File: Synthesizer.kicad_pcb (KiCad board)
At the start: 6 copper layers, 135.2 x 94.2 mm, 155 parts, among them J1 USB_A, J2 AudioJack3, J3 USB_B_Micro, J4 FPGA_debug, J5 MCU_debug, J6 MCU_GPIO, J7 FPGA_GPIO, SW1 SW_Push, SW10 SW_Push, SW11 SW_Push, SW12 SW_Push, SW13 SW_Push, SW14 SW_Push, SW15 SW_Push, SW16 SW_Push, SW2 SW_Push, SW3 SW_Push, SW4 SW_Push, SW5 SW_Push, SW6 SW_Push, SW7 SW_Push, SW8 SW_Push, SW9 SW_Push, U1 TPD3S014, U2 S25FL127S, U3 XC7A100T-FTG256, U4 Oscillator, U5 TPS54325, U6 TPS54294, U7 EFM32GG11B4xx, U8 PCM5102, Y1 48Mhz

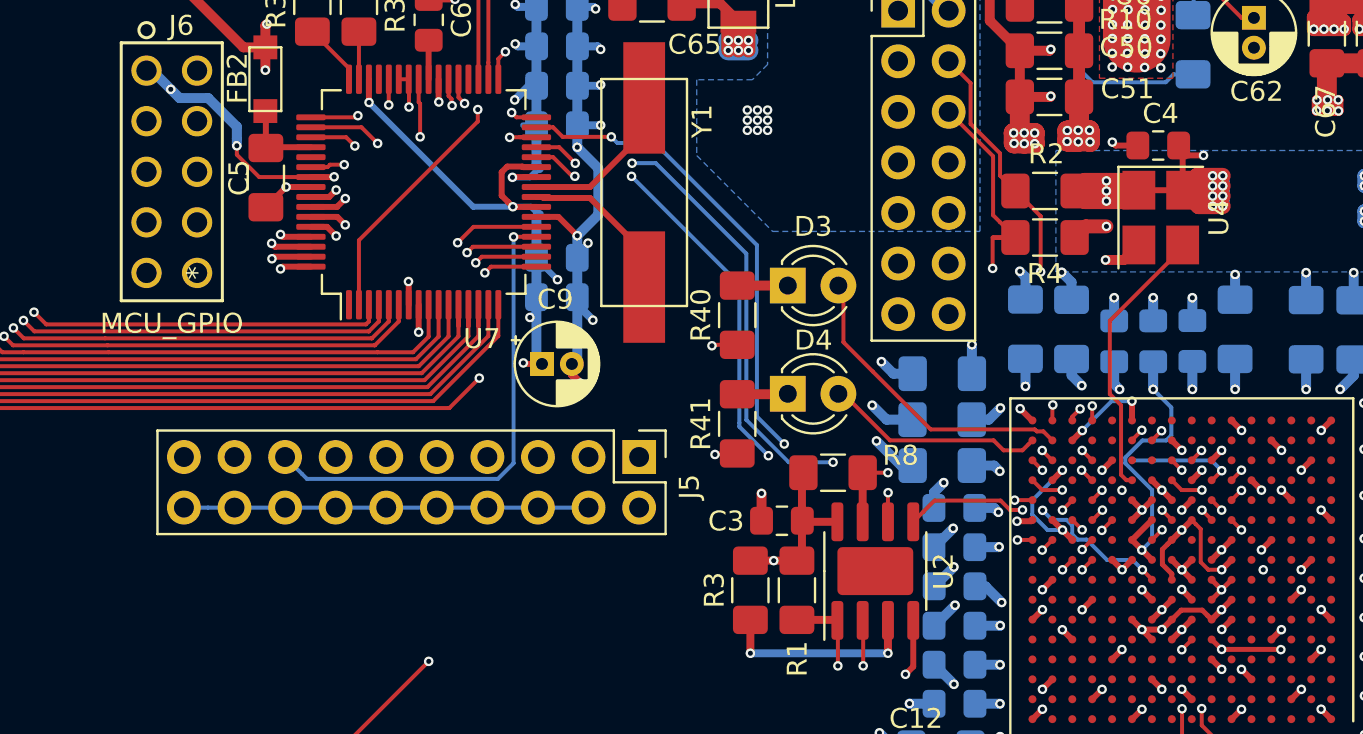
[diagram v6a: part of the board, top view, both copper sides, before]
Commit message: Thicken traces and thin planes
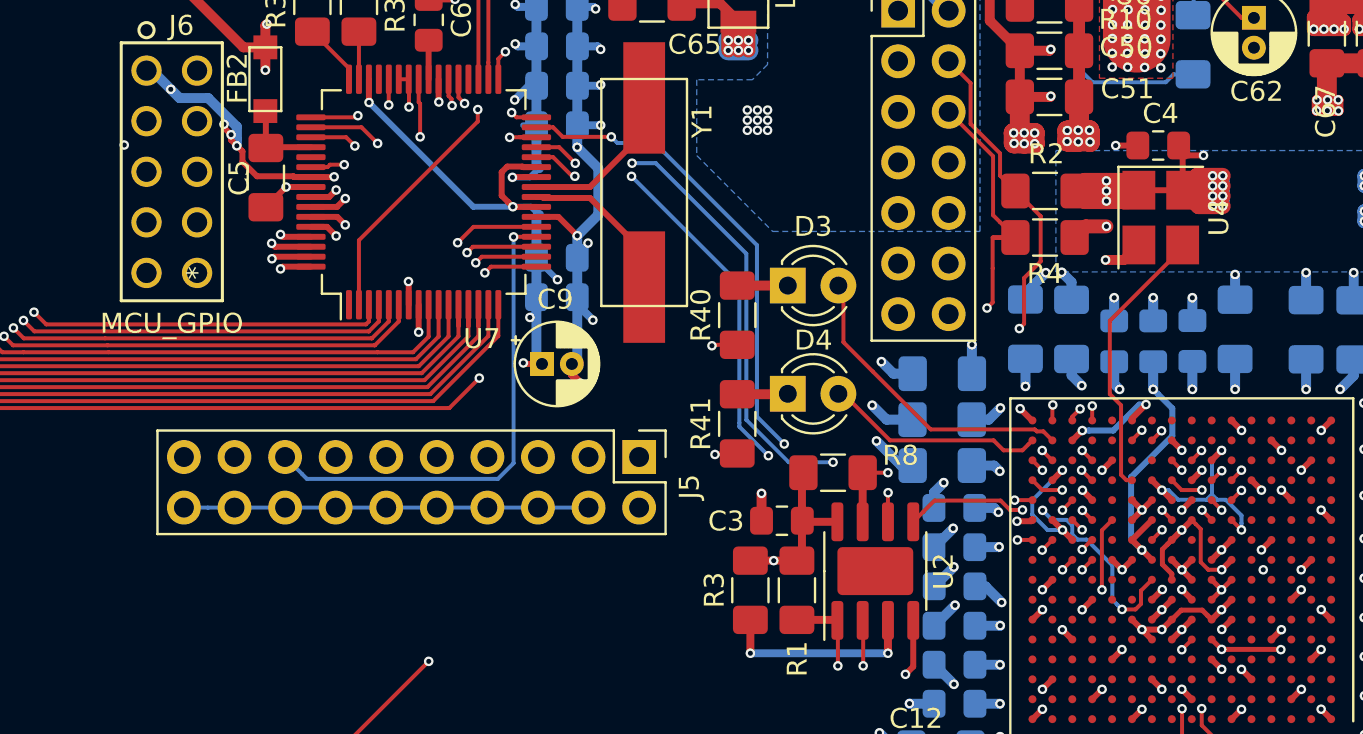
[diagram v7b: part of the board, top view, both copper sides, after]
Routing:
- net +3V3: track 504.1 -> 526.4 mm, vias 119 -> 122
- net Net-(J4-Pad10): track 26.8 -> 22.1 mm
- net +1V8: track 51.3 -> 48.9 mm
- net Net-(J4-Pad8): track 23.7 -> 22.2 mm
- net Net-(J4-Pad4): track 32.3 -> 31.0 mm
- net /Artix7/DAC_LRCK: track 49.2 -> 50.2 mm
- net /EFM32/FPGA_Ready: track 59.6 -> 60.2 mm
- net Net-(R1-Pad2): track 23.1 -> 23.7 mm
- net Net-(J4-Pad6): track 31.1 -> 31.3 mm, vias 3 -> 2

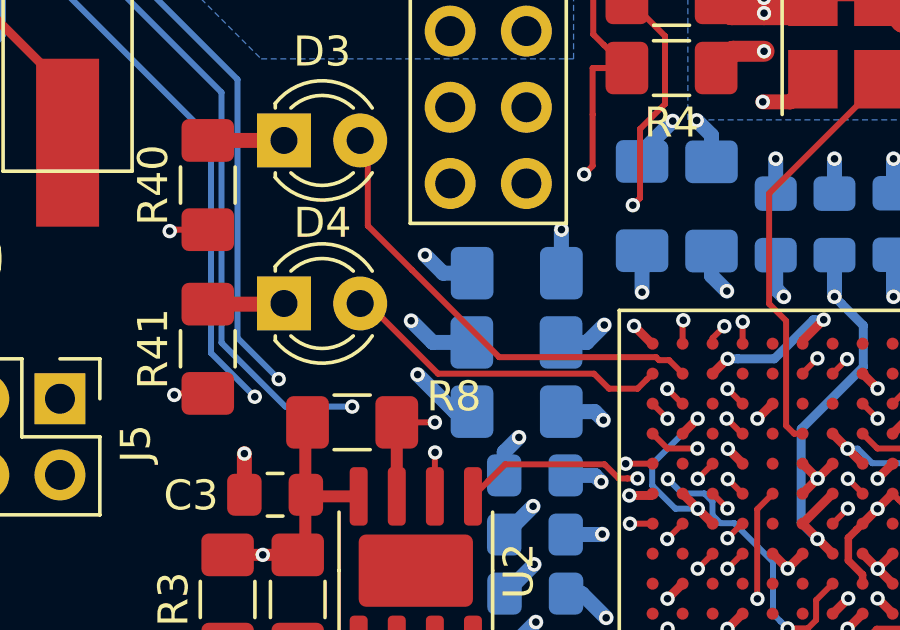
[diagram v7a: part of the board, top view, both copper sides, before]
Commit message: Thicken 1.8V layer
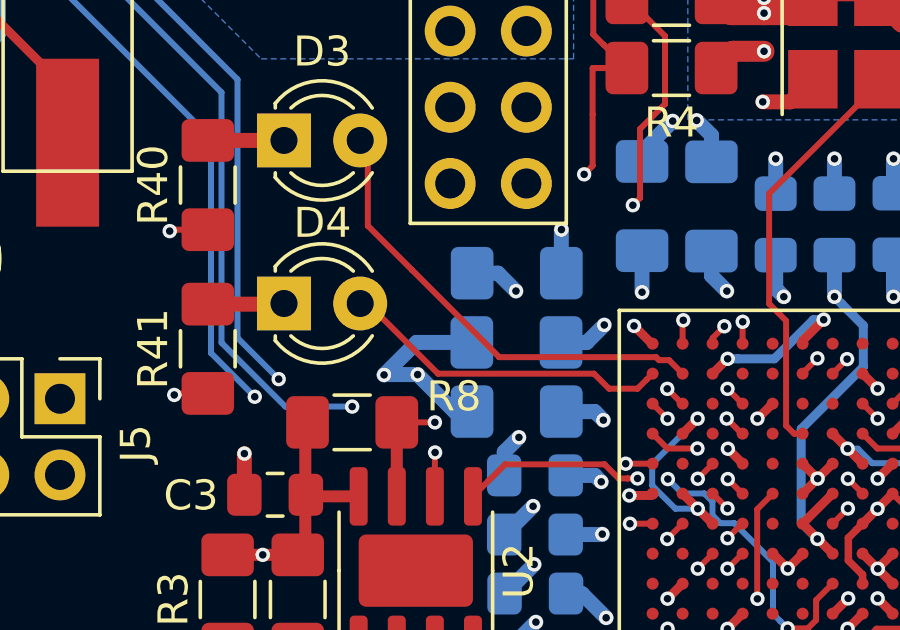
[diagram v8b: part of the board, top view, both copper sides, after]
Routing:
- net GND: track 360.0 -> 362.1 mm
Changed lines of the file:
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@@
     (thickness 1.6)
     (drawings 4)
-    (tracks 2591)
+    (tracks 2593)
     (zones 0)
     (modules 155)
@@
   (segment (start 138.27148 91.34856) (end 138.27996 91.35704) (width 0.3) (layer F.Cu) (net 2))
   (segment (start 138.22796 86.36254) (end 137.11682 86.36254) (width 0.3) (layer F.Cu) (net 2))
-  (via (at 125.35154 97.2185) (size 0.48) (drill 0.25) (layers F.Cu B.Cu) (net 2))
-  (segment (start 126.9206 97.82048) (end 125.95352 97.82048) (width 0.5) (layer B.Cu) (net 2))
-  (segment (start 125.95352 97.82048) (end 125.35154 97.2185) (width 0.5) (layer B.Cu) (net 2))
-  (via (at 124.888417 99.407295) (size 0.48) (drill 0.25) (layers F.Cu B.Cu) (net 2))
-  (segment (start 126.91044 100.12934) (end 125.610462 100.12934) (width 0.5) (layer B.Cu) (net 2))
-  (segment (start 125.610462 100.12934) (end 124.888417 99.407295) (width 0.5) (layer B.Cu) (net 2))
   (via (at 125.10516 101.20122) (size 0.48) (drill 0.25) (layers F.Cu B.Cu) (net 2))
   (segment (start 126.91806 102.43566) (end 126.3396 102.43566) (width 0.5) (layer B.Cu) (net 2))
@@
   (segment (start 132.58546 94.09618) (end 132.58546 93.77172) (width 0.5) (layer B.Cu) (net 2))
   (segment (start 132.58546 93.77172) (end 133.60654 92.75064) (width 0.5) (layer B.Cu) (net 2))
+  (via (at 128.38176 98.41738) (size 0.48) (drill 0.25) (layers F.Cu B.Cu) (net 2))
+  (segment (start 126.9206 97.82048) (end 127.78486 97.82048) (width 0.5) (layer B.Cu) (net 2))
+  (segment (start 127.78486 97.82048) (end 128.38176 98.41738) (width 0.5) (layer B.Cu) (net 2))
+  (via (at 123.98502 101.21138) (size 0.48) (drill 0.25) (layers F.Cu B.Cu) (net 2))
+  (segment (start 126.91044 100.12934) (end 125.06706 100.12934) (width 0.5) (layer B.Cu) (net 2))
+  (segment (start 125.06706 100.12934) (end 123.98502 101.21138) (width 0.5) (layer B.Cu) (net 2))
+  (segment (start 123.99518 101.20122) (end 123.98502 101.21138) (width 0.5) (layer B.Cu) (net 2))
+  (segment (start 125.10516 101.20122) (end 123.99518 101.20122) (width 0.5) (layer B.Cu) (net 2))
   (via (at 106.840151 89.438199) (size 0.48) (drill 0.25) (layers F.Cu B.Cu) (net 3))
   (segment (start 108.0245 89.4468) (end 106.848752 89.4468) (width 0.3) (layer F.Cu) (net 3))
@@
         (xy 143.51 111.252) (xy 143.51 116.332) (xy 146.558 116.332) (xy 146.558 116.84) (xy 146.558 121.158)
         (xy 146.558 121.666) (xy 127 121.666) (xy 127 121.158) (xy 127 103.886) (xy 127 103.124)
-        (xy 119.888 103.124) (xy 116.84 103.124) (xy 113.538 99.822) (xy 113.538 91.694) (xy 113.538 91.186)
-        (xy 121.158 91.186) (xy 121.158 90.678) (xy 121.158 84.836) (xy 118.872 82.55) (xy 114.046 82.55)
-        (xy 114.046 81.788) (xy 114.046 75.946) (xy 114.046 75.438) (xy 120.65 75.438) (xy 121.666 74.422)
-        (xy 121.666 68.834) (xy 120.142 67.31) (xy 120.142 65.278)
+        (xy 119.888 103.124) (xy 116.84 103.124) (xy 113.538 99.822) (xy 113.538 91.81592) (xy 121.158 88.28024)
+        (xy 121.158 84.836) (xy 118.872 82.55) (xy 114.046 82.55) (xy 114.046 81.788) (xy 114.046 75.946)
+        (xy 114.046 75.438) (xy 120.65 75.438) (xy 121.666 74.422) (xy 121.666 68.834) (xy 120.142 67.31)
+        (xy 120.142 65.278)
       )
     )
@@
         (xy 144.018 111.252) (xy 144.018 115.824) (xy 147.066 115.824) (xy 147.066 122.174) (xy 126.492 122.174)
         (xy 126.492 121.412) (xy 126.492 104.14) (xy 126.492 103.632) (xy 116.586 103.632) (xy 113.03 100.076)
-        (xy 113.03 91.44) (xy 113.03 90.678) (xy 120.65 90.678) (xy 120.65 90.17) (xy 120.65 85.09)
-        (xy 118.618 83.058) (xy 113.538 83.058) (xy 113.538 82.042) (xy 113.538 75.438) (xy 96.012 75.438)
-        (xy 96.012 83.82) (xy 92.456 83.82)
+        (xy 113.03 91.44) (xy 120.65 87.80526) (xy 120.65 85.09) (xy 118.618 83.058) (xy 113.538 83.058)
+        (xy 113.538 82.042) (xy 113.538 75.438) (xy 96.012 75.438) (xy 96.012 83.82) (xy 92.456 83.82)
       )
     )
